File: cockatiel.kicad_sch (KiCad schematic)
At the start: 44 parts

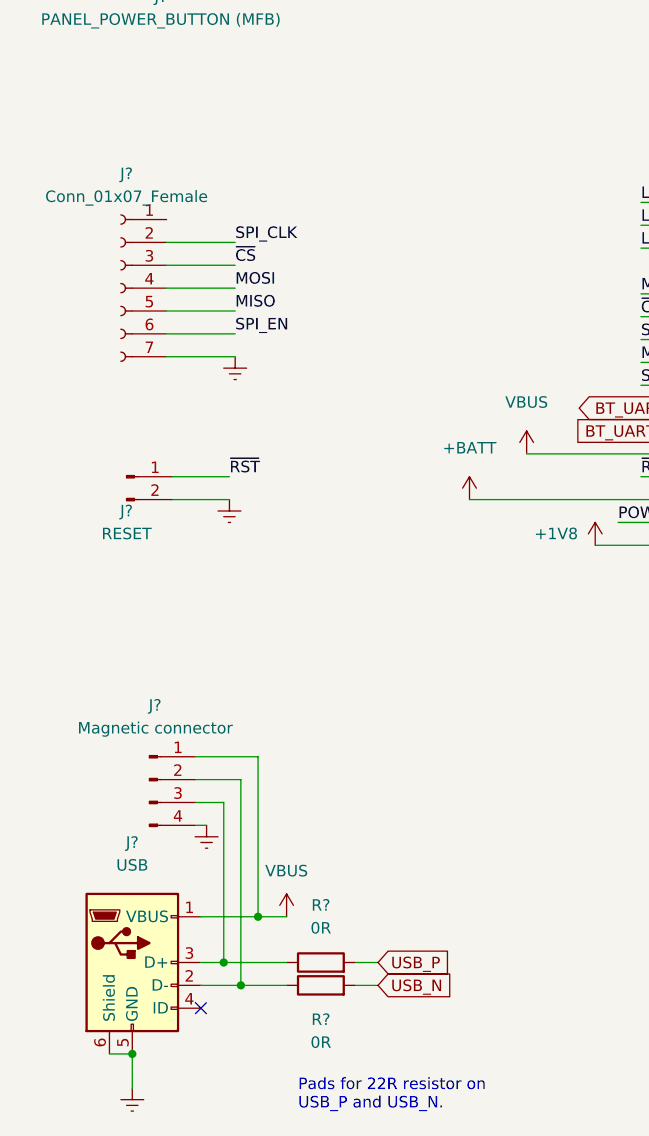
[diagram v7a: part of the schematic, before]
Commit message: Correct alignment of symbols on circuit diagram
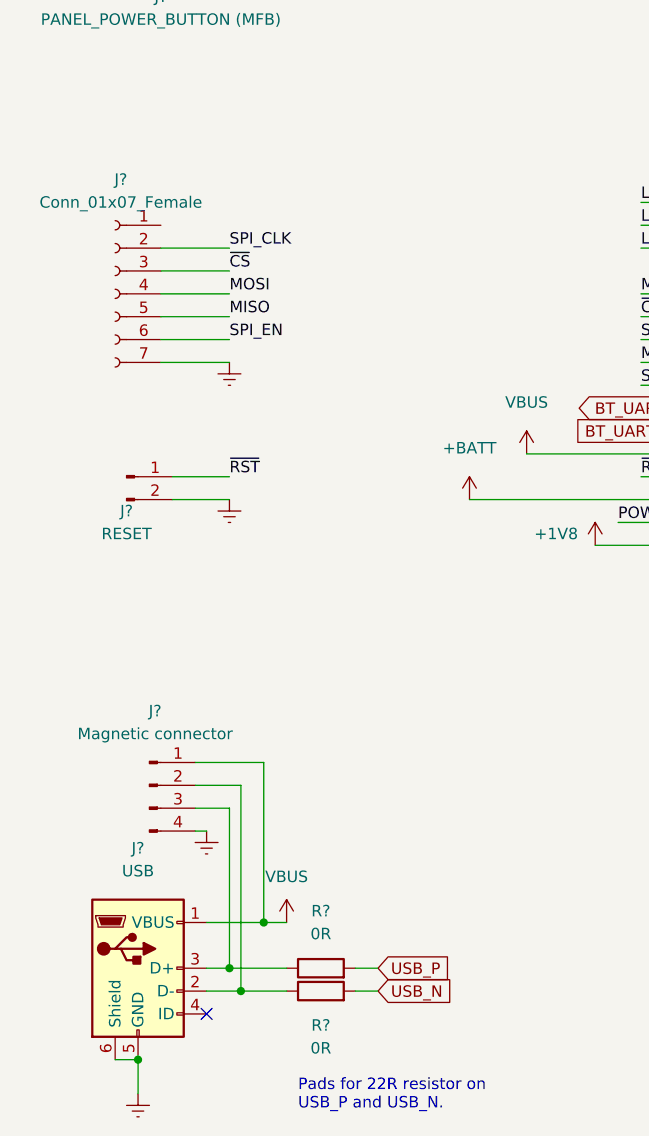
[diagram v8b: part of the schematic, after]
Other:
- moved on the sheet: J?, R?
